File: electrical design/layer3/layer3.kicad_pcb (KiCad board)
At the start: 2 copper layers, 150 x 137.9 mm, 41 parts, among them J1 SH1.0 5P, J10 SH1.0 2P, J11 LAYER1, J12 XH2.54 2P, J2 SH1.0 5P, J3 SH1.0 5P, J4 SH1.0 5P, J5 XH2.54 5P, J6 CAMERA1, J7 CAMERA2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

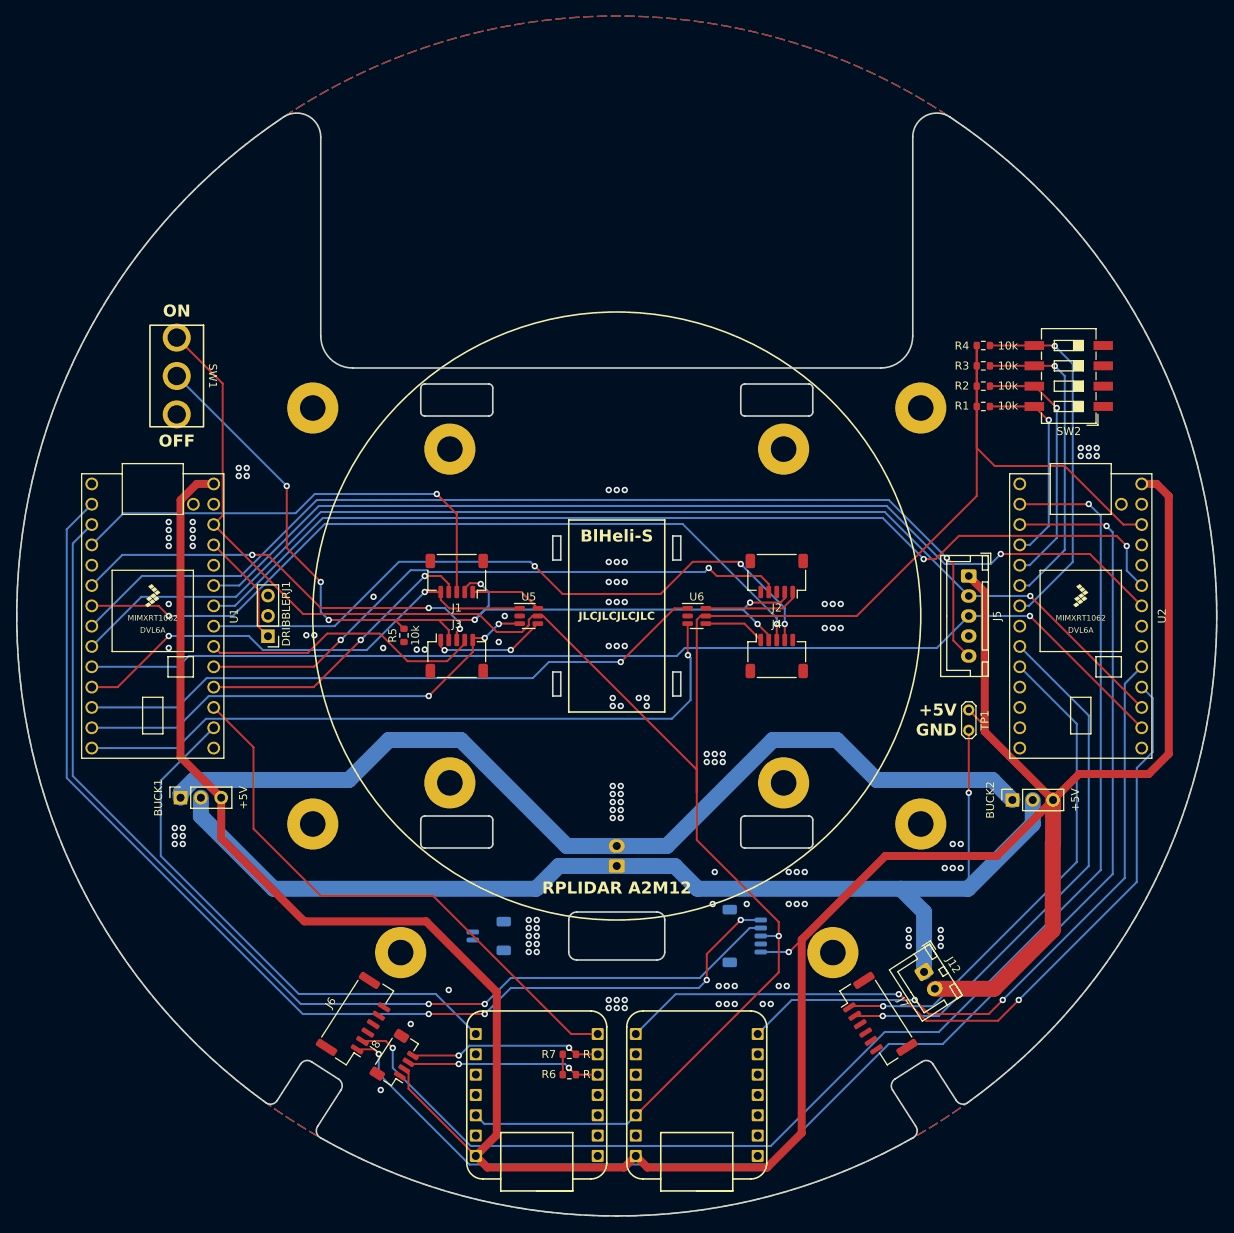
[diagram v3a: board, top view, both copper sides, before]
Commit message: add ducc finishes and route unconnected l3 items
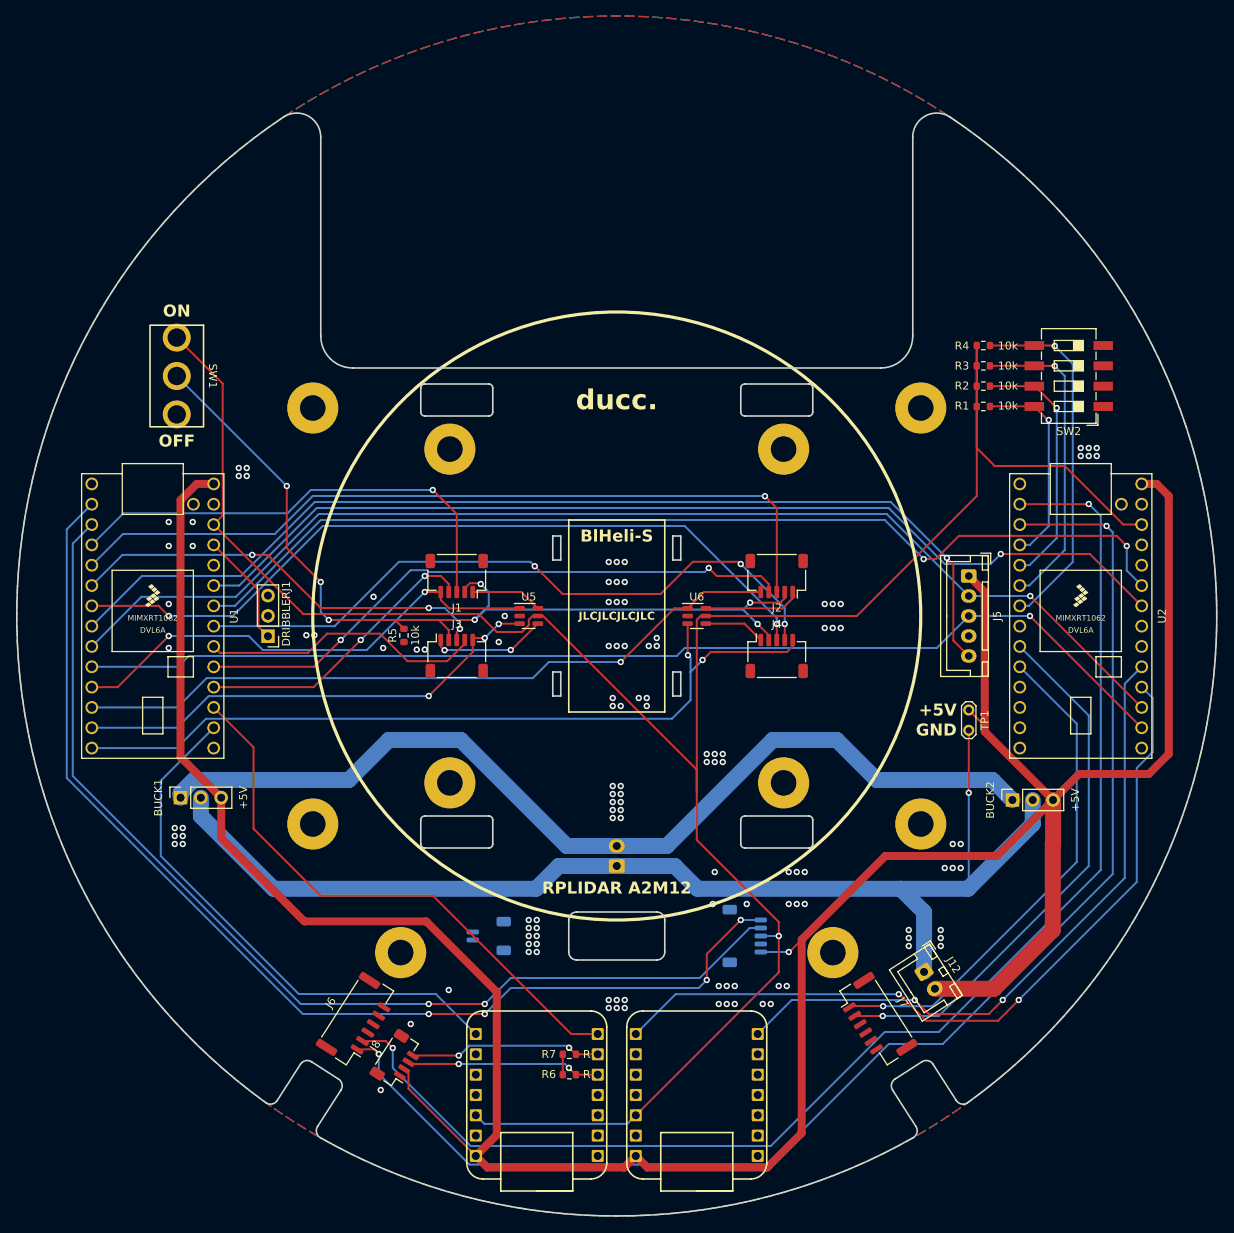
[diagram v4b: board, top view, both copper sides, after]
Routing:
- net /M2PWM: track 0.00 -> 100.6 mm, vias 0 -> 1
- net /M4INA: track 87.0 -> 101.9 mm, vias 1 -> 2
- net /M2INA: track 79.6 -> 89.6 mm
- net GNDD: vias 126 -> 122

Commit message: finalise pcbs for production
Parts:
- added G***: LOGO, LOGO, F.Cu at (105.0, 80.0)
- J11: value LAYER1 -> SH1.0 5P
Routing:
- net /CAM1RX: track 171.7 -> 0.00 mm, vias 2 -> 0
- net /CAM1TX: track 168.5 -> 0.00 mm, vias 2 -> 0
- net /BTTX: track 99.0 -> 0.00 mm, vias 2 -> 0
- net /BTRX: track 82.7 -> 0.00 mm, vias 2 -> 0
- net +5V: track 363.2 -> 315.9 mm
